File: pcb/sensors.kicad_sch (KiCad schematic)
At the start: 6 parts

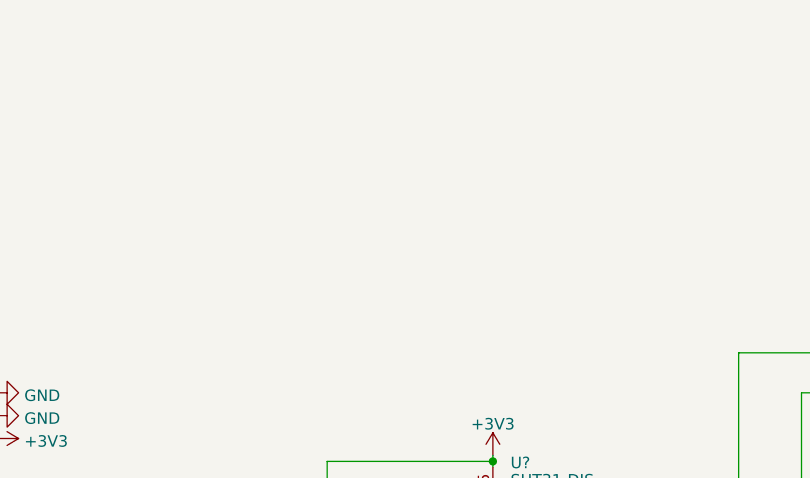
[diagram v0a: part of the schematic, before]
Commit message: Increase PCB size and fix EPD pinout
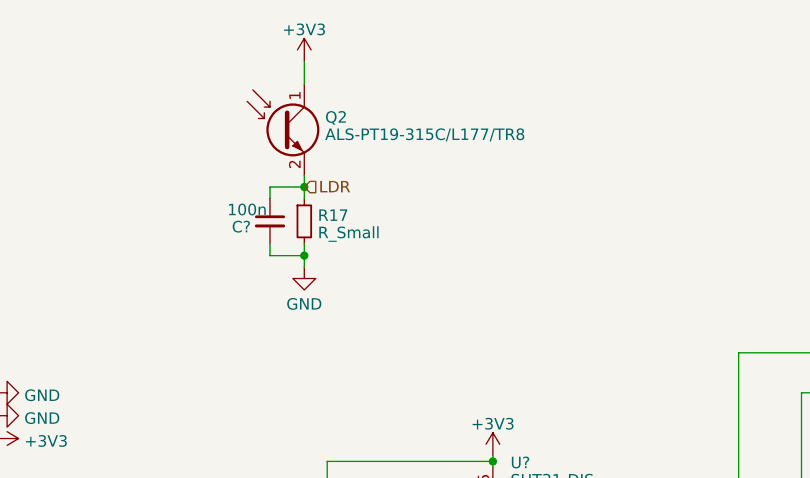
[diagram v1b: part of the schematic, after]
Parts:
- added C?: 100n, Capacitor_SMD:C_0603_1608Metric, symbol Device:C_Small
- added Q2: ALS-PT19-315C/L177/TR8, LED_SMD:LED_0603_1608Metric, symbol Sensor_Optical:TEPT4400
- added R17: R_Small, Resistor_SMD:R_0603_1608Metric, symbol Device:R_Small
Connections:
- net +3V3: now also Q2.1 (C)
- net GND: now also C?.2, R17.2
- new net LDR: C?.1, Q2.2 (E), R17.1
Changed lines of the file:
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@@
   (junction (at 150.495 86.36) (diameter 0) (color 0 0 0 0)
+  )
+  (junction (at 129.54 55.88) (diameter 0) (color 0 0 0 0)
+  )
+  (junction (at 129.54 63.5) (diameter 0) (color 0 0 0 0)
   )
   (junction (at 194.31 78.74) (diameter 0) (color 0 0 0 0)
@@
   (no_connect (at 140.335 94.615))
   (no_connect (at 160.655 97.155))
+  (wire (pts (xy 129.54 63.5) (xy 129.54 62.23))
+    (stroke (width 0) (type default))
+  )
+  (wire (pts (xy 129.54 64.77) (xy 129.54 63.5))
+    (stroke (width 0) (type default))
+  )
   (wire (pts (xy 150.495 86.36) (xy 150.495 86.995))
     (stroke (width 0) (type default))
@@
     (stroke (width 0) (type default))
   )
+  (wire (pts (xy 129.54 57.15) (xy 129.54 55.88))
+    (stroke (width 0) (type default))
+  )
   (wire (pts (xy 177.8 95.885) (xy 177.8 113.665))
     (stroke (width 0) (type default))
@@
     (stroke (width 0) (type default))
   )
+  (wire (pts (xy 129.54 55.88) (xy 129.54 54.61))
+    (stroke (width 0) (type default))
+  )
+  (wire (pts (xy 125.73 57.15) (xy 125.73 55.88))
+    (stroke (width 0) (type default))
+  )
+  (wire (pts (xy 125.73 63.5) (xy 129.54 63.5))
+    (stroke (width 0) (type default))
+  )
   (wire (pts (xy 184.785 109.22) (xy 194.31 109.22))
     (stroke (width 0) (type default))
@@
     (stroke (width 0) (type default))
   )
+  (wire (pts (xy 129.54 41.91) (xy 129.54 44.45))
+    (stroke (width 0) (type default))
+  )
+  (wire (pts (xy 125.73 55.88) (xy 129.54 55.88))
+    (stroke (width 0) (type default))
+  )
   (wire (pts (xy 184.785 90.805) (xy 184.785 78.74))
     (stroke (width 0) (type default))
   )
+  (wire (pts (xy 125.73 62.23) (xy 125.73 63.5))
+    (stroke (width 0) (type default))
+  )
   (wire (pts (xy 132.08 86.36) (xy 150.495 86.36))
     (stroke (width 0) (type default))
@@
   (wire (pts (xy 199.39 113.665) (xy 199.39 109.22))
     (stroke (width 0) (type default))
+  )
+  (hierarchical_label "LDR" (shape input) (at 129.54 55.88 0) (fields_autoplaced)
+    (effects (font (size 1.27 1.27)) (justify left))
   )
   (hierarchical_label "SCL" (shape input) (at 54.61 99.06 180) (fields_autoplaced)
@@
         (path "/df5fb727-aab3-46b2-bf4f-cd58d6f76ee2/7393a54f-26da-4d6d-9dc4-ee77d396380d"
           (reference "#PWR057") (unit 1)
+        )
+      )
+    )
+  )
+  (symbol (lib_id "Device:C_Small") (at 125.73 59.69 0) (mirror y) (unit 1)
+    (in_bom yes) (on_board yes) (dnp no)
+    (property "Reference" "C?" (at 122.555 60.325 0)
+      (effects (font (size 1.27 1.27)))
+    )
+    (property "Value" "100n" (at 123.19 58.42 0)
+      (effects (font (size 1.27 1.27)))
+    )
+    (property "Footprint" "Capacitor_SMD:C_0603_1608Metric" (at 125.73 59.69 0)
+      (effects (font (size 1.27 1.27)) hide)
+    )
+    (property "Datasheet" "~" (at 125.73 59.69 0)
+      (effects (font (size 1.27 1.27)) hide)
+    )
+    (pin "1")
+    (pin "2")
+    (instances
+      (project "RoomSensor"
+        (path "/df5fb727-aab3-46b2-bf4f-cd58d6f76ee2"
+          (reference "C?") (unit 1)
+        )
+        (path "/df5fb727-aab3-46b2-bf4f-cd58d6f76ee2/7393a54f-26da-4d6d-9dc4-ee77d396380d"
+          (reference "C15") (unit 1)
         )
       )
@@
         (path "/df5fb727-aab3-46b2-bf4f-cd58d6f76ee2/7393a54f-26da-4d6d-9dc4-ee77d396380d"
           (reference "C23") (unit 1)
+        )
+      )
+    )
+  )
+  (symbol (lib_id "Device:R_Small") (at 129.54 59.69 0) (unit 1)
+    (in_bom yes) (on_board yes) (dnp no) (fields_autoplaced)
+    (property "Reference" "R17" (at 131.0386 59.0463 0)
+      (effects (font (size 1.27 1.27)) (justify left))
+    )
+    (property "Value" "R_Small" (at 131.0386 60.9673 0)
+      (effects (font (size 1.27 1.27)) (justify left))
+    )
+    (property "Footprint" "Resistor_SMD:R_0603_1608Metric" (at 129.54 59.69 0)
+      (effects (font (size 1.27 1.27)) hide)
+    )
+    (property "Datasheet" "~" (at 129.54 59.69 0)
+      (effects (font (size 1.27 1.27)) hide)
+    )
+    (pin "1")
+    (pin "2")
+    (instances
+      (project "RoomSensor"
+        (path "/df5fb727-aab3-46b2-bf4f-cd58d6f76ee2/7393a54f-26da-4d6d-9dc4-ee77d396380d"
+          (reference "R17") (unit 1)
         )
       )
@@
         (path "/df5fb727-aab3-46b2-bf4f-cd58d6f76ee2/7393a54f-26da-4d6d-9dc4-ee77d396380d"
           (reference "#PWR053") (unit 1)
+        )
+      )
+    )
+  )
+  (symbol (lib_id "power:GND") (at 129.54 64.77 0) (unit 1)
+    (in_bom yes) (on_board yes) (dnp no) (fields_autoplaced)
+    (property "Reference" "#PWR?" (at 129.54 71.12 0)
+      (effects (font (size 1.27 1.27)) hide)
+    )
+    (property "Value" "GND" (at 129.54 68.9055 0)
+      (effects (font (size 1.27 1.27)))
+    )
+    (property "Footprint" "" (at 129.54 64.77 0)
+      (effects (font (size 1.27 1.27)) hide)
+    )
+    (property "Datasheet" "" (at 129.54 64.77 0)
+      (effects (font (size 1.27 1.27)) hide)
+    )
+    (pin "1")
+    (instances
+      (project "RoomSensor"
+        (path "/df5fb727-aab3-46b2-bf4f-cd58d6f76ee2"
+          (reference "#PWR?") (unit 1)
+        )
+        (path "/df5fb727-aab3-46b2-bf4f-cd58d6f76ee2/7393a54f-26da-4d6d-9dc4-ee77d396380d"
+          (reference "#PWR061") (unit 1)
         )
       )
@@
         (path "/df5fb727-aab3-46b2-bf4f-cd58d6f76ee2/7393a54f-26da-4d6d-9dc4-ee77d396380d"
           (reference "U7") (unit 1)
+        )
+      )
+    )
+  )
+  (symbol (lib_id "Sensor_Optical:TEPT4400") (at 127 49.53 0) (unit 1)
+    (in_bom yes) (on_board yes) (dnp no) (fields_autoplaced)
+    (property "Reference" "Q2" (at 131.8514 48.137 0)
+      (effects (font (size 1.27 1.27)) (justify left))
+    )
+    (property "Value" "ALS-PT19-315C/L177/TR8" (at 131.8514 50.058 0)
+      (effects (font (size 1.27 1.27)) (justify left))
+    )
+    (property "Footprint" "LED_SMD:LED_0603_1608Metric" (at 139.192 53.086 0)
+      (effects (font (size 1.27 1.27)) hide)
+    )
+    (property "Datasheet" "https://datasheet.lcsc.com/lcsc/1806131537_Everlight-Elec-ALS-PT19-315C-L177-TR8_C146233.pdf" (at 127 49.53 0)
+      (effects (font (size 1.27 1.27)) hide)
+    )
+    (pin "1")
+    (pin "2")
+    (instances
+      (project "RoomSensor"
+        (path "/df5fb727-aab3-46b2-bf4f-cd58d6f76ee2/7393a54f-26da-4d6d-9dc4-ee77d396380d"
+          (reference "Q2") (unit 1)
         )
       )
@@
         )
       )
+    )
+  )
+  (symbol (lib_id "power:+3V3") (at 129.54 41.91 0) (unit 1)
+    (in_bom yes) (on_board yes) (dnp no) (fields_autoplaced)
+    (property "Reference" "#PWR?" (at 129.54 45.72 0)
+      (effects (font (size 1.27 1.27)) hide)
+    )
+    (property "Value" "+3V3" (at 129.54 38.4081 0)
+      (effects (font (size 1.27 1.27)))
+    )
+    (property "Footprint" "" (at 129.54 41.91 0)
+      (effects (font (size 1.27 1.27)) hide)
+    )
+    (property "Datasheet" "" (at 129.54 41.91 0)
+      (effects (font (size 1.27 1.27)) hide)
+    )
+    (pin "1")
+    (instances
+      (project "RoomSensor"
+        (path "/df5fb727-aab3-46b2-bf4f-cd58d6f76ee2"
+          (reference "#PWR?") (unit 1)
+        )
+        (path "/df5fb727-aab3-46b2-bf4f-cd58d6f76ee2/7393a54f-26da-4d6d-9dc4-ee77d396380d"
+          (reference "#PWR062") (unit 1)
+        )
+      )

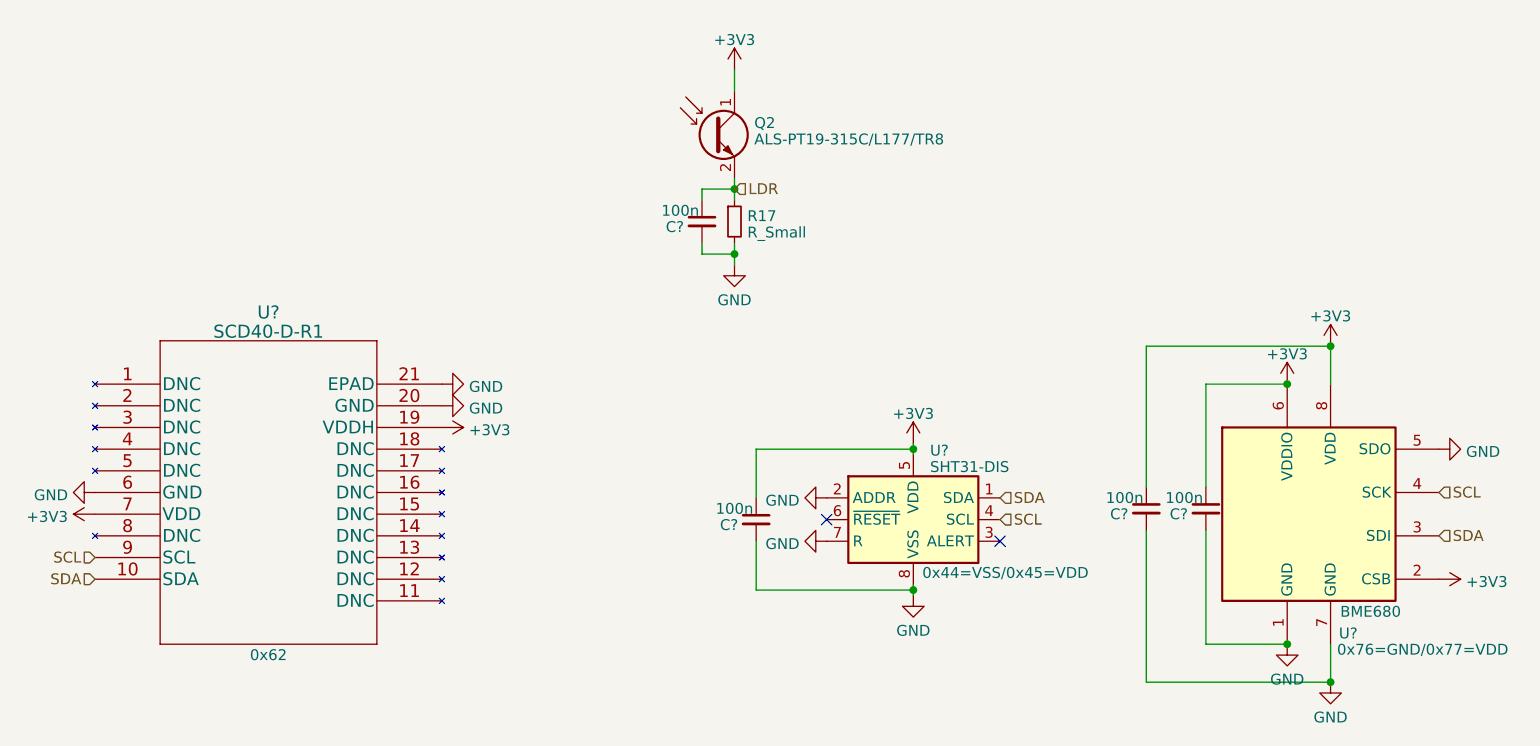
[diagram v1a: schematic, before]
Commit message: Fix low power issues
- Fix spurious EPD wakeups by adding pull-up to EPD reset line
- Reduce power consumption by switching sensors off with mosfet
- Connect button to reset to reduce power by not needing rtc gpio
- Add solder jumper for silent boot
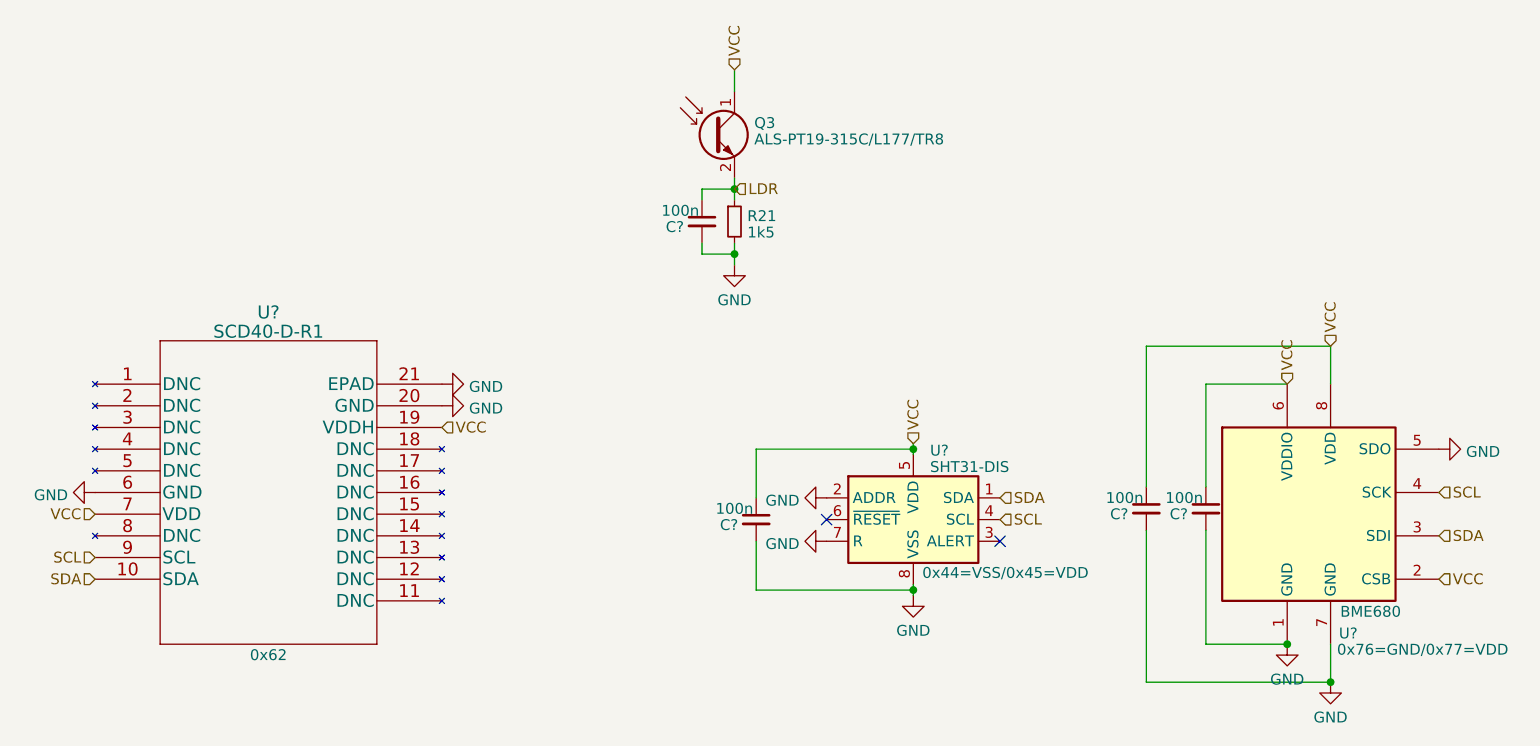
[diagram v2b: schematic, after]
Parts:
- R21: renamed from R17; value R_Small -> 1k5
- renumbered Q2 to Q3
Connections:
- net +3V3 renamed VCC
